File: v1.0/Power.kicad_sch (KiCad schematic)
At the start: 41 parts, among them J1 BATT_XT60, Q1 DMG2301L, U2 TPS63060, U3 SPX3819M5-L-3-3

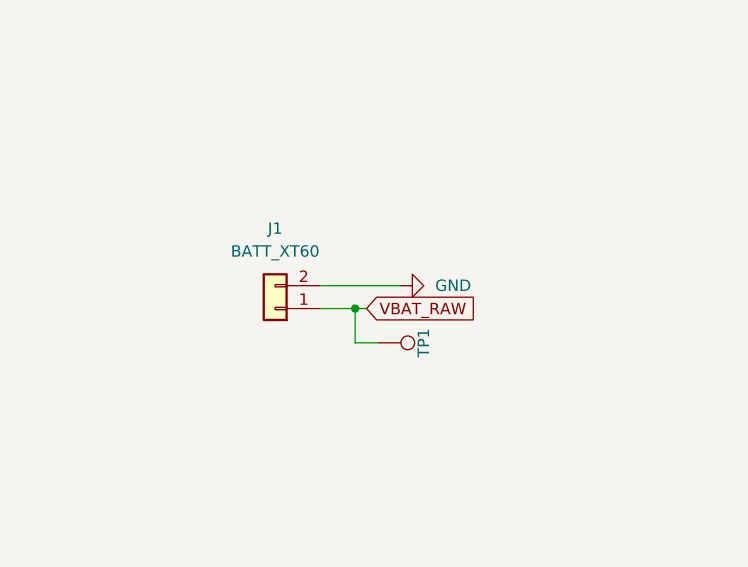
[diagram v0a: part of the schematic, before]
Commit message: v1.0: update schematics and PCB layout
Co-Authored-By: Claude Opus 4.7 (1M context) <noreply@anthropic.com>
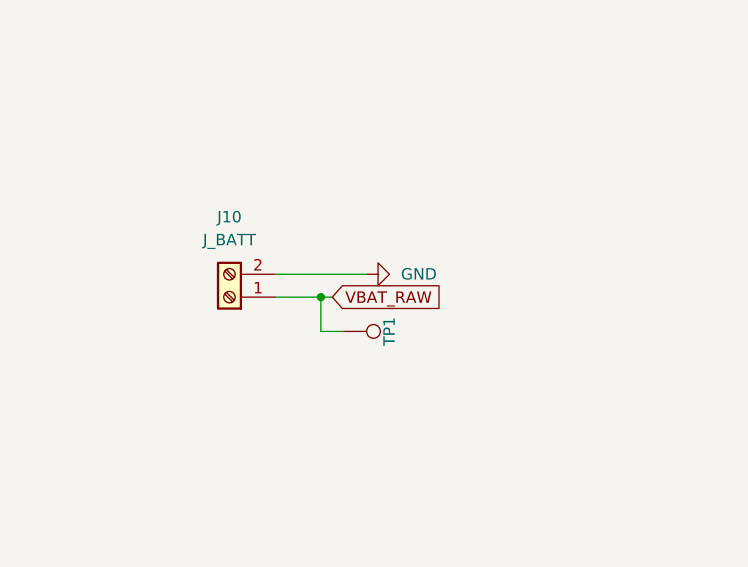
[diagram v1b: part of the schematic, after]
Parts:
- removed J1: BATT_XT60, Connector_AMASS:AMASS_XT60PW-M_1x02_P7.20mm_Horizontal, symbol Connector_Generic:Conn_01x02
- added J10: J_BATT, TerminalBlock_Phoenix:TerminalBlock_Phoenix_MKDS-1,5-2-5.08_1x02_P5.08mm_Horizontal, symbol Connector:Screw_Terminal_01x02
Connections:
- net GND: now also J10.2 (Pin_2)
- net VBAT_RAW: now also J10.1 (Pin_1)
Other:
- moved on the sheet: TP1
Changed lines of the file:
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@@
 	)
 	(junction
-		(at 72.39 54.61)
-		(diameter 0)
-		(color 0 0 0 0)
-	)
-	(junction
 		(at 180.34 130.81)
 		(diameter 0)
@@
 	)
 	(junction
+		(at 68.58 53.34)
+		(diameter 0)
+		(color 0 0 0 0)
+	)
+	(junction
 		(at 100.33 119.38)
 		(diameter 0)
@@
 	(wire
 		(pts
-			(xy 68.58 54.61) (xy 72.39 54.61)
+			(xy 63.5 53.34) (xy 68.58 53.34)
 		)
 		(stroke
@@
 	(wire
 		(pts
-			(xy 72.39 54.61) (xy 73.66 54.61)
+			(xy 68.58 53.34) (xy 69.85 53.34)
 		)
 		(stroke
@@
 	(wire
 		(pts
-			(xy 72.39 58.42) (xy 72.39 54.61)
+			(xy 68.58 57.15) (xy 68.58 53.34)
 		)
 		(stroke
@@
 	(wire
 		(pts
-			(xy 68.58 52.07) (xy 77.47 52.07)
+			(xy 63.5 50.8) (xy 73.66 50.8)
 		)
 		(stroke
@@
 	(wire
 		(pts
-			(xy 74.93 58.42) (xy 72.39 58.42)
+			(xy 71.12 57.15) (xy 68.58 57.15)
 		)
 		(stroke
@@
 	(global_label "VBAT_RAW"
 		(shape input)
-		(at 73.66 54.61 0)
+		(at 69.85 53.34 0)
 		(fields_autoplaced yes)
 		(effects
@@
 		)
 		(property "Intersheetrefs" "${INTERSHEET_REFS}"
-			(at 85.8376 54.61 0)
+			(at 82.0276 53.34 0)
 			(hide yes)
 			(show_name no)
@@
 	)
 	(symbol
+		(lib_id "Connector:Screw_Terminal_01x02")
+		(at 58.42 53.34 180)
+		(unit 1)
+		(body_style 1)
+		(exclude_from_sim no)
+		(in_bom yes)
+		(on_board yes)
+		(in_pos_files yes)
+		(dnp no)
+		(fields_autoplaced yes)
+		(property "Reference" "J10"
+			(at 58.42 44.45 0)
+			(show_name no)
+			(do_not_autoplace no)
+			(effects
+				(font
+					(size 1.27 1.27)
+				)
+			)
+		)
+		(property "Value" "J_BATT"
+			(at 58.42 46.99 0)
+			(show_name no)
+			(do_not_autoplace no)
+			(effects
+				(font
+					(size 1.27 1.27)
+				)
+			)
+		)
+		(property "Footprint" "TerminalBlock_Phoenix:TerminalBlock_Phoenix_MKDS-1,5-2-5.08_1x02_P5.08mm_Horizontal"
+			(at 58.42 53.34 0)
+			(hide yes)
+			(show_name no)
+			(do_not_autoplace no)
+			(effects
+				(font
+					(size 1.27 1.27)
+				)
+			)
+		)
+		(property "Datasheet" ""
+			(at 58.42 53.34 0)
+			(hide yes)
+			(show_name no)
+			(do_not_autoplace no)
+			(effects
+				(font
+					(size 1.27 1.27)
+				)
+			)
+		)
+		(property "Description" "Generic screw terminal, single row, 01x02, script generated (kicad-library-utils/schlib/autogen/connector/)"
+			(at 58.42 53.34 0)
+			(hide yes)
+			(show_name no)
+			(do_not_autoplace no)
+			(effects
+				(font
+					(size 1.27 1.27)
+				)
+			)
+		)
+		(pin "2"
+		)
+		(pin "1"
+		)
+		(instances
+			(project "UNSW_Rocketry_Senior_Flight_Computer"
+				(path "/9e0253f5-fba5-4205-8256-7fc47a91dd1e/32dc7f8f-d1cd-4967-8830-7944681bf161"
+					(reference "J10")
+					(unit 1)
+				)
+			)
+		)
+	)
+	(symbol
 		(lib_id "power:+3.3V")
 		(at 107.95 151.13 270)
@@
 	(symbol
 		(lib_id "PCM_SparkFun-Connector:TestPoint_1.0mm")
-		(at 74.93 58.42 270)
+		(at 71.12 57.15 270)
 		(unit 1)
 		(body_style 1)
@@
 		(fields_autoplaced yes)
 		(property "Reference" "TP1"
-			(at 80.01 58.42 0)
+			(at 76.2 57.15 0)
 			(show_name no)
 			(do_not_autoplace yes)
@@
 		)
 		(property "Value" "1.0mm"
-			(at 71.12 58.42 0)
+			(at 67.31 57.15 0)
 			(hide yes)
 			(show_name no)
@@
 		)
 		(property "Footprint" "PCM_SparkFun-Connector:TestPoint-1.0mm"
-			(at 68.58 58.42 0)
+			(at 64.77 57.15 0)
 			(hide yes)
 			(show_name no)
@@
 		)
 		(property "Datasheet" ""
-			(at 67.31 58.42 0)
+			(at 63.5 57.15 0)
 			(hide yes)
 			(show_name no)
@@
 		)
 		(property "Description" "Test Point"
-			(at 64.77 58.42 0)
+			(at 60.96 57.15 0)
 			(hide yes)
 			(show_name no)
@@
 	)
 	(symbol
-		(lib_id "Connector_Generic:Conn_01x02")
-		(at 63.5 54.61 180)
-		(unit 1)
-		(body_style 1)
-		(exclude_from_sim no)
-		(in_bom yes)
-		(on_board yes)
-		(in_pos_files yes)
-		(dnp no)
-		(fields_autoplaced yes)
-		(property "Reference" "J1"
-			(at 63.5 45.72 0)
-			(show_name no)
-			(do_not_autoplace no)
-			(effects
-				(font
-					(size 1.27 1.27)
-				)
-			)
-		)
-		(property "Value" "BATT_XT60"
-			(at 63.5 48.26 0)
-			(show_name no)
-			(do_not_autoplace no)
-			(effects
-				(font
-					(size 1.27 1.27)
-				)
-			)
-		)
-		(property "Footprint" "Connector_AMASS:AMASS_XT60PW-M_1x02_P7.20mm_Horizontal"
-			(at 63.5 54.61 0)
-			(hide yes)
-			(show_name no)
-			(do_not_autoplace no)
-			(effects
-				(font
-					(size 1.27 1.27)
-				)
-			)
-		)
-		(property "Datasheet" ""
-			(at 63.5 54.61 0)
-			(hide yes)
-			(show_name no)
-			(do_not_autoplace no)
-			(effects
-				(font
-					(size 1.27 1.27)
-				)
-			)
-		)
-		(property "Description" "Generic connector, single row, 01x02, script generated (kicad-library-utils/schlib/autogen/connector/)"
-			(at 63.5 54.61 0)
-			(hide yes)
-			(show_name no)
-			(do_not_autoplace no)
-			(effects
-				(font
-					(size 1.27 1.27)
-				)
-			)
-		)
-		(pin "1"
-		)
-		(pin "2"
-		)
-		(instances
-			(project "UNSW_Rocketry_Senior_Flight_Computer"
-				(path "/9e0253f5-fba5-4205-8256-7fc47a91dd1e/32dc7f8f-d1cd-4967-8830-7944681bf161"
-					(reference "J1")
-					(unit 1)
-				)
-			)
-		)
-	)
-	(symbol
 		(lib_id "power:GND")
 		(at 191.77 107.95 180)
@@
 	(symbol
 		(lib_id "power:GND")
-		(at 77.47 52.07 90)
+		(at 73.66 50.8 90)
 		(unit 1)
 		(body_style 1)
@@
 		(fields_autoplaced yes)
 		(property "Reference" "#PWR024"
-			(at 83.82 52.07 0)
+			(at 80.01 50.8 0)
 			(hide yes)
 			(show_name no)
@@
 		)
 		(property "Value" "GND"
-			(at 81.28 52.0699 90)
+			(at 77.47 50.7999 90)
 			(show_name no)
 			(do_not_autoplace no)
@@
 		)
 		(property "Footprint" ""
-			(at 77.47 52.07 0)
+			(at 73.66 50.8 0)
 			(hide yes)
 			(show_name no)
@@
 		)
 		(property "Datasheet" ""
-			(at 77.47 52.07 0)
+			(at 73.66 50.8 0)
 			(hide yes)
 			(show_name no)
@@
 		)
 		(property "Description" "Power symbol creates a global label with name \"GND\" , ground"
-			(at 77.47 52.07 0)
+			(at 73.66 50.8 0)
 			(hide yes)
 			(show_name no)

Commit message: v1.0: update Power/Pyros schematics and PCB; add JUNO_XL and Untitled_2 footprints
Co-Authored-By: Claude Opus 4.8 (1M context) <noreply@anthropic.com>
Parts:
- J10: footprint TerminalBlock_Phoenix:TerminalBlock_Phoenix_MKDS-1,5-2-5.08_1x02_P5.08mm_Horizontal -> TerminalBlock_Phoenix:TerminalBlock_Phoenix_PT-1,5-2-3.5-H_1x02_P3.50mm_Horizontal
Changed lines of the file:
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@@
 			)
 		)
-		(property "Footprint" "TerminalBlock_Phoenix:TerminalBlock_Phoenix_MKDS-1,5-2-5.08_1x02_P5.08mm_Horizontal"
+		(property "Footprint" "TerminalBlock_Phoenix:TerminalBlock_Phoenix_PT-1,5-2-3.5-H_1x02_P3.50mm_Horizontal"
 			(at 58.42 53.34 0)
 			(hide yes)
